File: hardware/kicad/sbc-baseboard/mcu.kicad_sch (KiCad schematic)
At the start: 41 parts, among them J16 SWD, J3 USB-C HID to target, SW201 RESET, U201 MK64FN1M0VLL12, U202 USBLC6-2SC6, Y201 32.768kHz

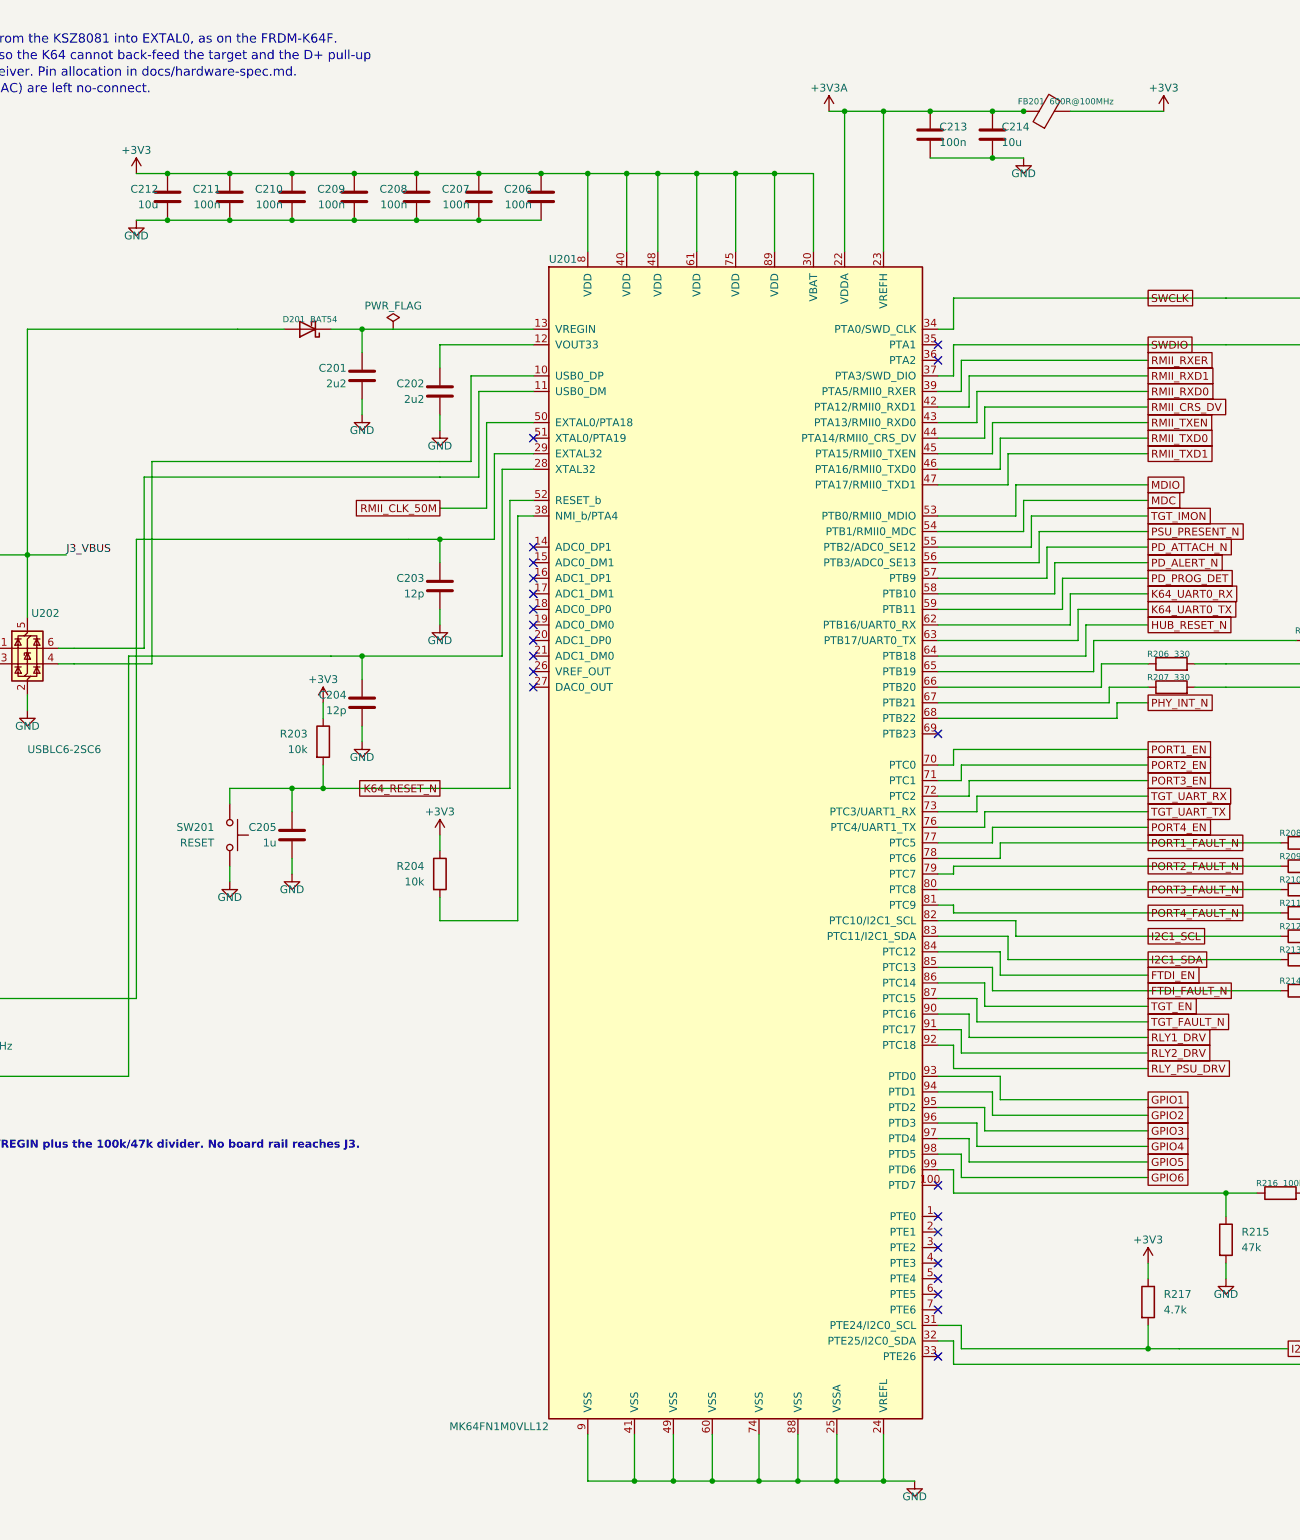
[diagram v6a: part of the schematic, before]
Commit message: House symbols from the ecad-libraries submodule
The project symbols move to calicopizzadelivery/ecad-libraries, added as a
submodule at hardware/kicad/libs and pinned to v0.1.1. The generator loads
them from the submodule's files (kisym.EXTRA_LIBS), so the embedded copies
match the library exactly; sym-lib-table and fp-lib-table are the fragments
the library ships, naming calico-ic and calico-electromechanical as
${KIPRJMOD}/../libs/... gen/parts.py and the project .kicad_sym are gone.

The symbols now follow the KiCad Library Conventions (every pin on the 100 mil
grid of the origin, 20 mil name offset), which moved a few pin rows; the port
blocks are re-aligned to the stacked USB-A's new rows. All sheets: ERC 0,
contacts 0, merges 0, layout 0; connectivity unchanged.

Co-Authored-By: Claude Fable 5.1 <noreply@anthropic.com>
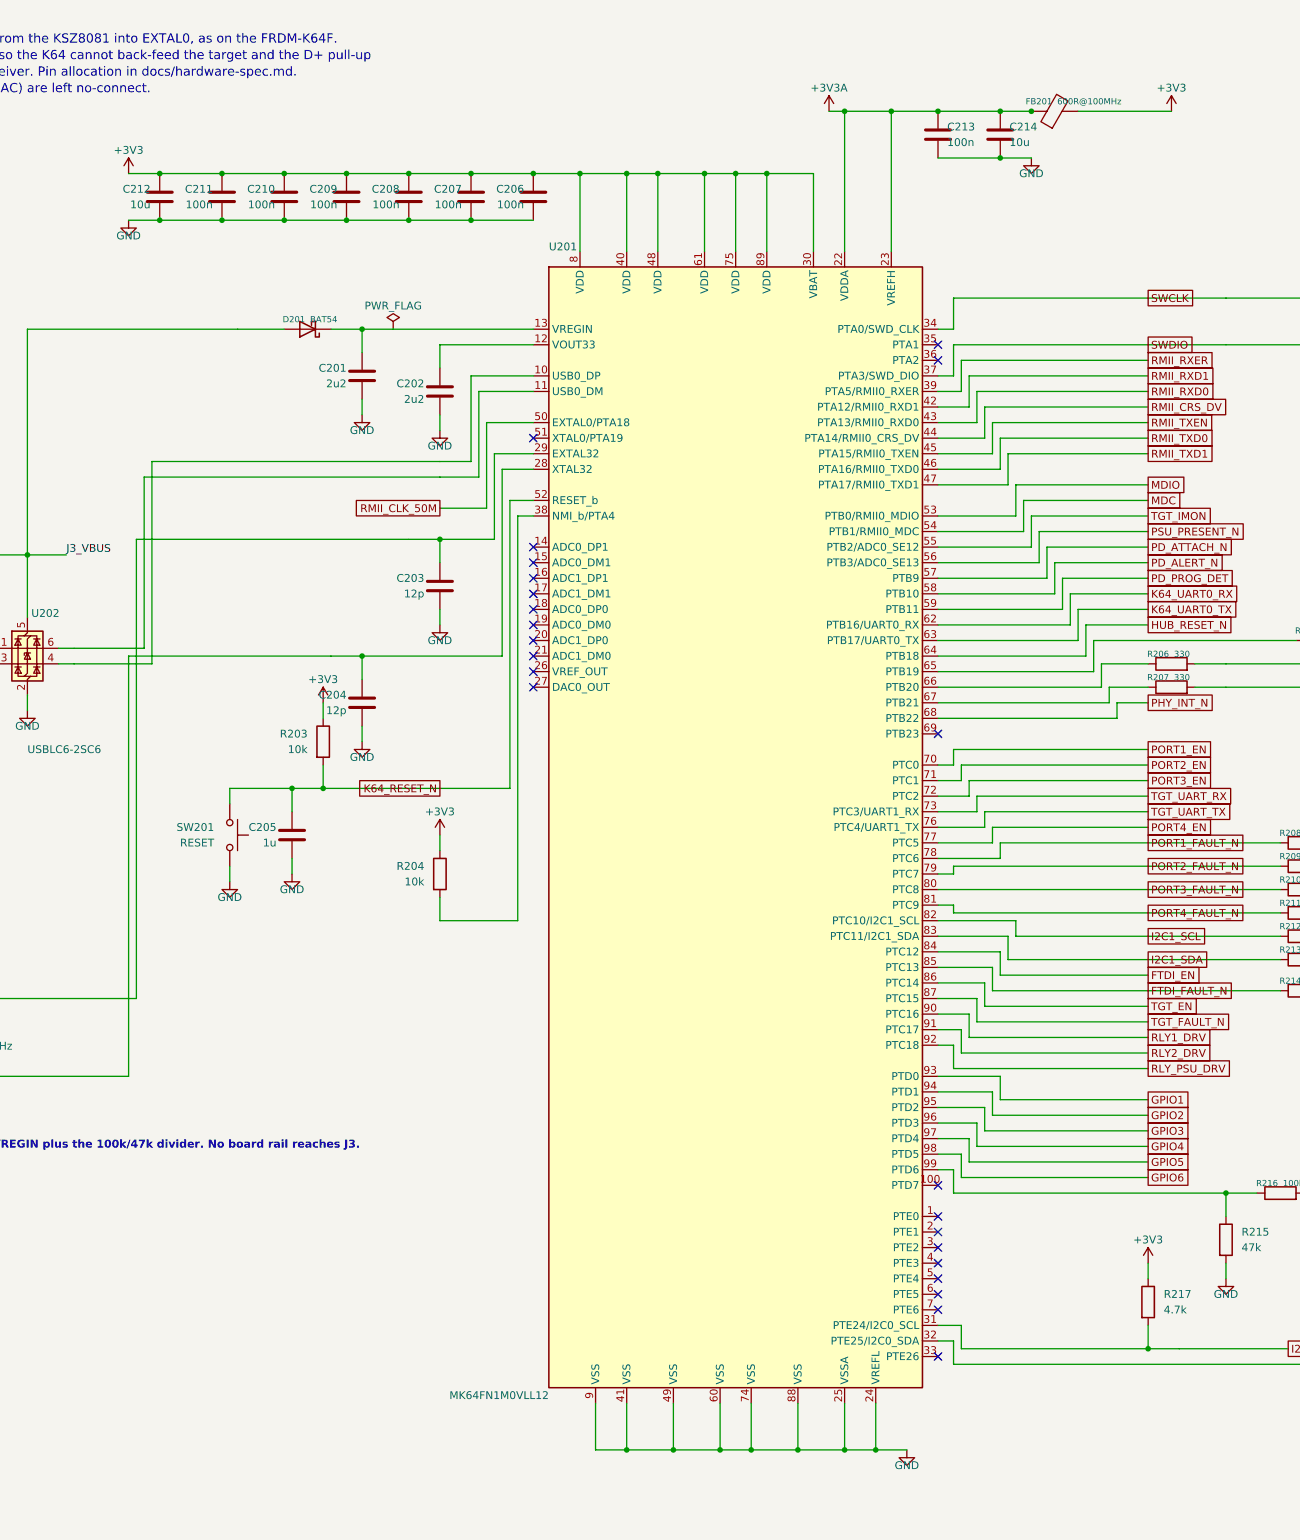
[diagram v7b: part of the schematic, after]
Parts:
- removed U201: MK64FN1M0VLL12, Package_QFP:LQFP-100_14x14mm_P0.5mm, symbol sbcbb:MK64FN1M0VLL12
- added U201: MK64FN1M0VLL12, Package_QFP:LQFP-100_14x14mm_P0.5mm, symbol calico-ic:MK64FN1M0VLL12
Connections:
- net +3V3: now also U201.30 (VBAT), U201.40 (VDD), U201.48 (VDD), U201.61 (VDD), U201.75 (VDD), U201.8 (VDD), U201.89 (VDD)
- net +3V3A: now also U201.22 (VDDA), U201.23 (VREFH)
- net FTDI_EN: now also U201.84 (PTC12)
- net FTDI_FAULT_N: now also U201.85 (PTC13)
- net GND: now also U201.24 (VREFL), U201.25 (VSSA), U201.41 (VSS), U201.49 (VSS), U201.60 (VSS), U201.74 (VSS), U201.88 (VSS), U201.9 (VSS)
- net GPIO1: now also U201.93 (PTD0)
- net GPIO2: now also U201.94 (PTD1)
- net GPIO3: now also U201.95 (PTD2)
- net GPIO4: now also U201.96 (PTD3)
- net GPIO5: now also U201.97 (PTD4)
- net GPIO6: now also U201.98 (PTD5)
- net HUB_RESET_N: now also U201.64 (PTB18)
- net I2C0_SCL: now also U201.31 (PTE24/I2C0_SCL)
- net I2C0_SDA: now also U201.32 (PTE25/I2C0_SDA)
- net I2C1_SCL: now also U201.82 (PTC10/I2C1_SCL)
- net I2C1_SDA: now also U201.83 (PTC11/I2C1_SDA)
- net K64_RESET_N: now also U201.52 (RESET_b)
- net K64_UART0_RX: now also U201.62 (PTB16/UART0_RX)
- net K64_UART0_TX: now also U201.63 (PTB17/UART0_TX)
- net MDC: now also U201.54 (PTB1/RMII0_MDC)
- net MDIO: now also U201.53 (PTB0/RMII0_MDIO)
- net PD_ALERT_N: now also U201.58 (PTB10)
- net PD_ATTACH_N: now also U201.57 (PTB9)
- net PD_PROG_DET: now also U201.59 (PTB11)
- net PHY_INT_N: now also U201.68 (PTB22)
- net PORT1_EN: now also U201.70 (PTC0)
- net PORT1_FAULT_N: now also U201.78 (PTC6)
- net PORT2_EN: now also U201.71 (PTC1)
- net PORT2_FAULT_N: now also U201.79 (PTC7)
- net PORT3_EN: now also U201.72 (PTC2)
- net PORT3_FAULT_N: now also U201.80 (PTC8)
- net PORT4_EN: now also U201.77 (PTC5)
- net PORT4_FAULT_N: now also U201.81 (PTC9)
- net PSU_PRESENT_N: now also U201.56 (PTB3/ADC0_SE13)
- net RLY1_DRV: now also U201.90 (PTC16)
- net RLY2_DRV: now also U201.91 (PTC17)
- net RLY_PSU_DRV: now also U201.92 (PTC18)
- net RMII_CLK_50M: now also U201.50 (EXTAL0/PTA18)
- net RMII_CRS_DV: now also U201.44 (PTA14/RMII0_CRS_DV)
- net RMII_RXD0: now also U201.43 (PTA13/RMII0_RXD0)
- net RMII_RXD1: now also U201.42 (PTA12/RMII0_RXD1)
- net RMII_RXER: now also U201.39 (PTA5/RMII0_RXER)
- net RMII_TXD0: now also U201.46 (PTA16/RMII0_TXD0)
- net RMII_TXD1: now also U201.47 (PTA17/RMII0_TXD1)
- net RMII_TXEN: now also U201.45 (PTA15/RMII0_TXEN)
- net SWCLK: now also U201.34 (PTA0/SWD_CLK)
- net SWDIO: now also U201.37 (PTA3/SWD_DIO)
- net TGT_EN: now also U201.86 (PTC14)
- net TGT_FAULT_N: now also U201.87 (PTC15)
- net TGT_IMON: now also U201.55 (PTB2/ADC0_SE12)
- net TGT_UART_RX: now also U201.73 (PTC3/UART1_RX)
- net TGT_UART_TX: now also U201.76 (PTC4/UART1_TX)
- net at C203.1, Y201.2: now also U201.29 (EXTAL32)
- net at C201.1, D201.1 (K): now also U201.13 (VREGIN)
- net at R206.1: now also U201.66 (PTB20)
- net at R205.1: now also U201.65 (PTB19)
- net at C204.1, Y201.1: now also U201.28 (XTAL32)
- net at R207.1: now also U201.67 (PTB21)
- net at R215.1, R216.1: now also U201.99 (PTD6)
- net at U202.4 (I/O2): now also U201.10 (USB0_DP)
- net at U202.6 (I/O1): now also U201.11 (USB0_DM)
- net at C202.1: now also U201.12 (VOUT33)
- net at R204.2: now also U201.38 (NMI_b/PTA4)
